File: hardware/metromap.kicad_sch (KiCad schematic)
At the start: 36 parts, among them J1 USB_C_Receptacle_USB2.0_16P, U1 AZ1117-3.3, U2 SN74LVC1G125DBV, U3 ESP32-C6-MINI-1-H4

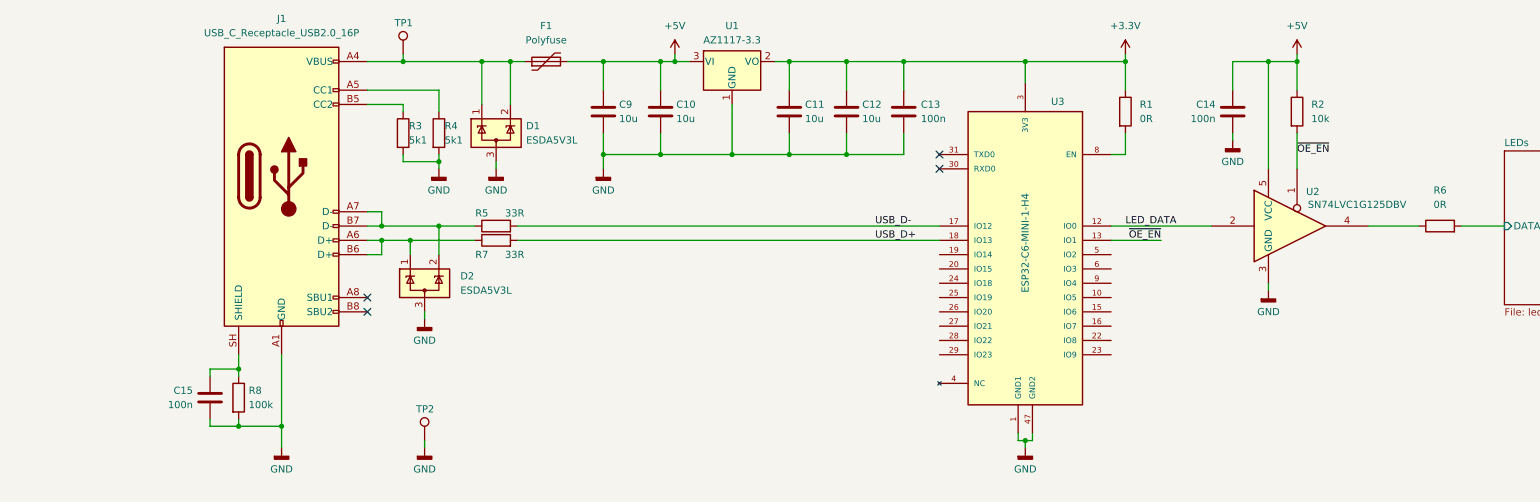
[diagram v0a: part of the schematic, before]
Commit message: Updated LED footprint
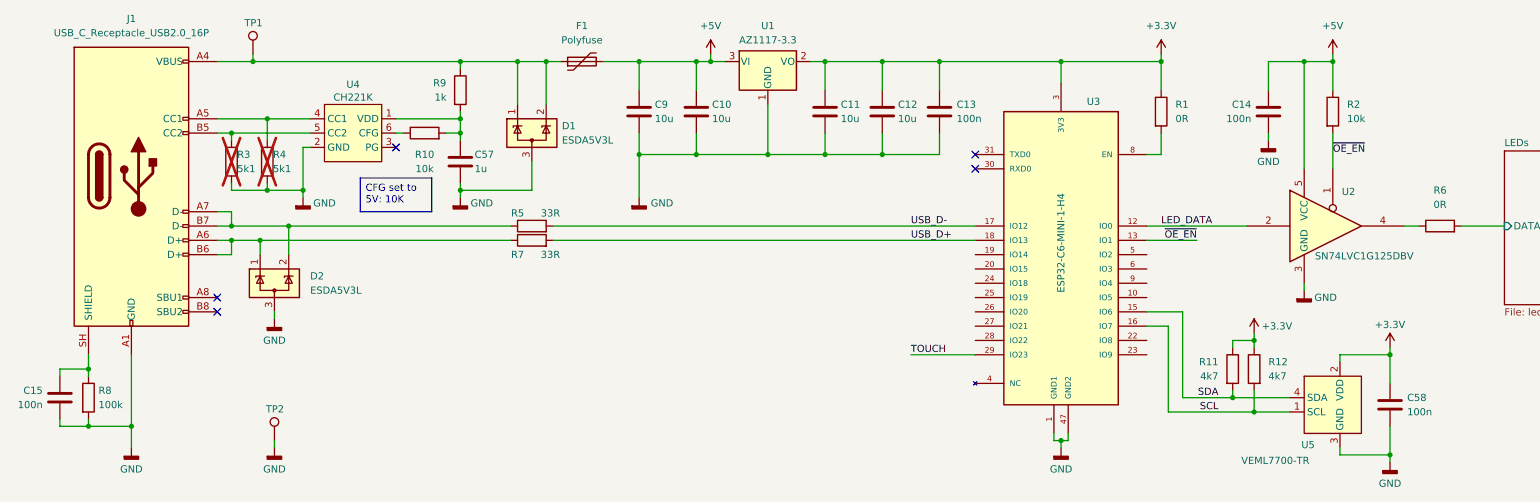
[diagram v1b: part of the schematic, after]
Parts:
- added C57: 1u, Capacitor_SMD:C_0603_1608Metric, symbol Device:C
- added C58: 100n, Capacitor_SMD:C_0402_1005Metric, symbol Device:C
- added R10: 10k, Resistor_SMD:R_0603_1608Metric, symbol Device:R
- added R11, R12: 4k7, Resistor_SMD:R_0603_1608Metric, symbol Device:R
- added R9: 1k, Resistor_SMD:R_0603_1608Metric, symbol Device:R
- added U4: CH221K, Package_TO_SOT_SMD:SOT-23-6, symbol metro-tracker:CH221K
- added U5: VEML7700-TR, metro-tracker:XDCR_VEML7700-TR, symbol metro-tracker:VEML7700-TR
- R3, R4: now not fitted
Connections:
- net +3.3V: now also C58.1, R11.1, R12.1, U5.2 (VDD)
- net GND: now also C57.2, C58.2, U4.2 (GND), U5.3 (GND)
- net at D1.1 (K), D1.2 (K), F1.1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: now also R9.1
- net at J1.A5 (CC1), R4.1: now also U4.4 (CC1)
- net at J1.B5 (CC2), R3.1: now also U4.5 (CC2)
- net SDA: now reaches U3.15 (IO6)
- net SDA: now also R11.2, U5.4 (SDA)
- net SCL: now reaches U3.16 (IO7)
- net SCL: now also R12.2, U5.1 (SCL)
- net TOUCH: now reaches U3.29 (IO23)
- new net: C57.1, R10.2, R9.2, U4.1 (VDD)
- new net: R10.1, U4.6 (CFG)
- no-connect marks 4 -> 5
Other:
- moved on the sheet: C10, C11, C12, C13, C14, C15, C9, D1, D2, F1, J1, R1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

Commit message: replaced buffer
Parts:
- removed U2: SN74LVC1G125DBV, Package_TO_SOT_SMD:SOT-23-5, symbol 74xGxx:SN74LVC1G125DBV
- added TP3, TP4: (no value), TestPoint:TestPoint_Pad_D2.0mm, symbol Connector:TestPoint
- added U2: SN74AHCT1G125DBVR, Package_TO_SOT_SMD:SOT-23-5, symbol metro-tracker:SN74AHCT1G125DBVR
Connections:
- net +5V: now also U2.5 (VCC)
- net GND: now also U2.3 (GND)
- net LED_DATA: now also U2.2
- net CON_USB_D+: now reaches J1.A6 (D+), J1.B6 (D+), R7.1
- net CON_USB_D+: now also D2.2 (K); no longer D2.1 (K)
- net CON_USB_D-: now reaches J1.A7 (D-), J1.B7 (D-), R5.1
- net CON_USB_D-: now also D2.1 (K); no longer D2.2 (K)
- net at R6.1: now also TP3.1, U2.4
- net ~{OE_EN} renamed ~{OE}
- net ~{OE}: now also TP4.1, U2.1

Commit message: Initial routing done
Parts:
- added C59: 47u, Capacitor_SMD:CP_Elec_6.3x7.7, symbol Device:C_Polarized
- C8: footprint Capacitor_SMD:CP_Elec_5x5.7 -> Capacitor_SMD:CP_Elec_6.3x7.7
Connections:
- net +5V: now also C59.1
- net GND: now also C59.2
- net VBUS: now reaches D1.1 (K), D1.2 (K), F1.1, J1.A4 (VBUS), J1.A9 (VBUS), J1.B4 (VBUS), J1.B9 (VBUS), R9.1, TP1.1
- net SH: now reaches C15.1, J1.SH (SHIELD), R8.1
- net TOUCH: no longer names the net of U3.29 (IO23)
- no-connect marks 5 -> 19
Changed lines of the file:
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@@
 	)
 	(no_connect
+		(at 186.69 109.22)
+	)
+	(no_connect
+		(at 186.69 101.6)
+	)
+	(no_connect
+		(at 186.69 93.98)
+	)
+	(no_connect
+		(at 217.17 96.52)
+	)
+	(no_connect
 		(at 186.69 76.2)
 	)
@@
 	)
 	(no_connect
+		(at 217.17 91.44)
+	)
+	(no_connect
+		(at 186.69 106.68)
+	)
+	(no_connect
+		(at 186.69 99.06)
+	)
+	(no_connect
+		(at 186.69 96.52)
+	)
+	(no_connect
 		(at 52.07 101.6)
 	)
 	(no_connect
+		(at 186.69 104.14)
+	)
+	(no_connect
+		(at 217.17 93.98)
+	)
+	(no_connect
+		(at 217.17 109.22)
+	)
+	(no_connect
 		(at 52.07 99.06)
 	)
 	(no_connect
+		(at 217.17 99.06)
+	)
+	(no_connect
+		(at 217.17 106.68)
+	)
+	(no_connect
+		(at 186.69 91.44)
+	)
+	(no_connect
 		(at 83.82 72.39)
 	)
@@
 	(wire
 		(pts
-			(xy 29.21 111.76) (xy 24.13 111.76)
+			(xy 389.89 68.58) (xy 389.89 69.85)
 		)
 		(stroke
@@
 	(wire
 		(pts
-			(xy 52.07 67.31) (xy 60.96 67.31)
+			(xy 29.21 111.76) (xy 24.13 111.76)
 		)
 		(stroke
@@
 	(wire
 		(pts
-			(xy 120.65 57.15) (xy 127 57.15)
+			(xy 52.07 67.31) (xy 60.96 67.31)
 		)
 		(stroke
@@
 	(wire
 		(pts
-			(xy 250.19 57.15) (xy 245.11 57.15)
+			(xy 120.65 57.15) (xy 127 57.15)
 		)
 		(stroke
@@
 	(wire
 		(pts
-			(xy 29.21 121.92) (xy 36.83 121.92)
+			(xy 250.19 57.15) (xy 245.11 57.15)
 		)
 		(stroke
@@
 	(wire
 		(pts
-			(xy 157.48 57.15) (xy 160.02 57.15)
+			(xy 29.21 121.92) (xy 36.83 121.92)
 		)
 		(stroke
@@
 	(wire
 		(pts
-			(xy 175.26 109.22) (xy 186.69 109.22)
+			(xy 157.48 57.15) (xy 160.02 57.15)
 		)
 		(stroke
@@
 	(wire
 		(pts
+			(xy 389.89 59.69) (xy 379.73 59.69)
+		)
+		(stroke
+			(width 0)
+			(type default)
+		)
+	)
+	(wire
+		(pts
 			(xy 52.07 86.36) (xy 54.61 86.36)
 		)
@@
 	(wire
 		(pts
+			(xy 389.89 69.85) (xy 379.73 69.85)
+		)
+		(stroke
+			(width 0)
+			(type default)
+		)
+	)
+	(wire
+		(pts
 			(xy 251.46 109.22) (xy 260.35 109.22)
 		)
@@
 		)
 	)
+	(wire
+		(pts
+			(xy 389.89 60.96) (xy 389.89 59.69)
+		)
+		(stroke
+			(width 0)
+			(type default)
+		)
+	)
 	(label "CON_USB_D-"
 		(at 69.85 86.36 0)
@@
 		)
 	)
-	(label "TOUCH"
-		(at 175.26 109.22 0)
-		(effects
-			(font
-				(size 1.27 1.27)
-			)
-			(justify left bottom)
-		)
-	)
 	(label "SDA"
 		(at 229.87 116.84 180)
@@
 		)
 	)
+	(label "SH"
+		(at 27.94 111.76 180)
+		(effects
+			(font
+				(size 1.27 1.27)
+			)
+			(justify right bottom)
+		)
+	)
+	(label "VBUS"
+		(at 63.5 57.15 0)
+		(effects
+			(font
+				(size 1.27 1.27)
+			)
+			(justify left bottom)
+		)
+	)
 	(label "~{OE}"
 		(at 250.19 74.93 0)
@@
 			)
 		)
-		(property "Footprint" "Capacitor_SMD:CP_Elec_5x5.7"
+		(property "Footprint" "Capacitor_SMD:CP_Elec_6.3x7.7"
 			(at 380.6952 68.58 0)
 			(hide yes)
@@
 					(unit 1)
 				)
+			)
+		)
+	)
+	(symbol
+		(lib_id "Device:C_Polarized")
+		(at 389.89 64.77 0)
+		(unit 1)
+		(body_style 1)
+		(exclude_from_sim no)
+		(in_bom yes)
+		(on_board yes)
+		(in_pos_files yes)
+		(dnp no)
+		(fields_autoplaced yes)
+		(property "Reference" "C59"
+			(at 393.7 62.6109 0)
+			(show_name no)
+			(do_not_autoplace no)
+			(effects
+				(font
+					(size 1.27 1.27)
+				)
+				(justify left)
+			)
+		)
+		(property "Value" "47u"
+			(at 393.7 65.1509 0)
+			(show_name no)
+			(do_not_autoplace no)
+			(effects
+				(font
+					(size 1.27 1.27)
+				)
+				(justify left)
+			)
+		)
+		(property "Footprint" "Capacitor_SMD:CP_Elec_6.3x7.7"
+			(at 390.8552 68.58 0)
+			(hide yes)
+			(show_name no)
+			(do_not_autoplace no)
+			(effects
+				(font
+					(size 1.27 1.27)
+				)
+			)
+		)
+		(property "Datasheet" ""
+			(at 389.89 64.77 0)
+			(hide yes)
+			(show_name no)
+			(do_not_autoplace no)
+			(effects
+				(font
+					(size 1.27 1.27)
+				)
+			)
+		)
+		(property "Description" "Polarized capacitor"
+			(at 389.89 64.77 0)
+			(hide yes)
+			(show_name no)
+			(do_not_autoplace no)
+			(effects
+				(font
+					(size 1.27 1.27)
+				)
+			)
+		)
+		(property "Digikey Part Number" "732-6390-1-ND"
+			(at 389.89 64.77 0)
+			(hide yes)
+			(show_name no)
+			(do_not_autoplace no)
+			(effects
+				(font
+					(size 1.27 1.27)
+				)
+			)
+		)
+		(property "JLCPCB Part Number" "C2161511"
+			(at 389.89 64.77 0)
+			(hide yes)
+			(show_name no)
+			(do_not_autoplace no)
+			(effects
+				(font
+					(size 1.27 1.27)
+				)
+			)
+		)
+		(property "Manufacturer Part Name JLCPCB" "16SVPG47M"
+			(at 389.89 64.77 0)
+			(hide yes)
+			(show_name no)
+			(do_not_autoplace no)
+			(effects
+				(font
+					(size 1.27 1.27)
+				)
+			)
+		)
+		(property "Manufacturer Part Number Digikey" "875105142001"
+			(at 389.89 64.77 0)
+			(hide yes)
+			(show_name no)
+			(do_not_autoplace no)
+			(effects
+				(font
+					(size 1.27 1.27)
+				)
+			)
+		)
+		(pin "1"
+		)
+		(pin "2"
+		)
+		(instances
+			(project "metromap"
+				(path "/933613dd-e874-4353-aa56-f5aedaa7dcf5"
+					(reference "C59")
+					(unit 1)
+				)

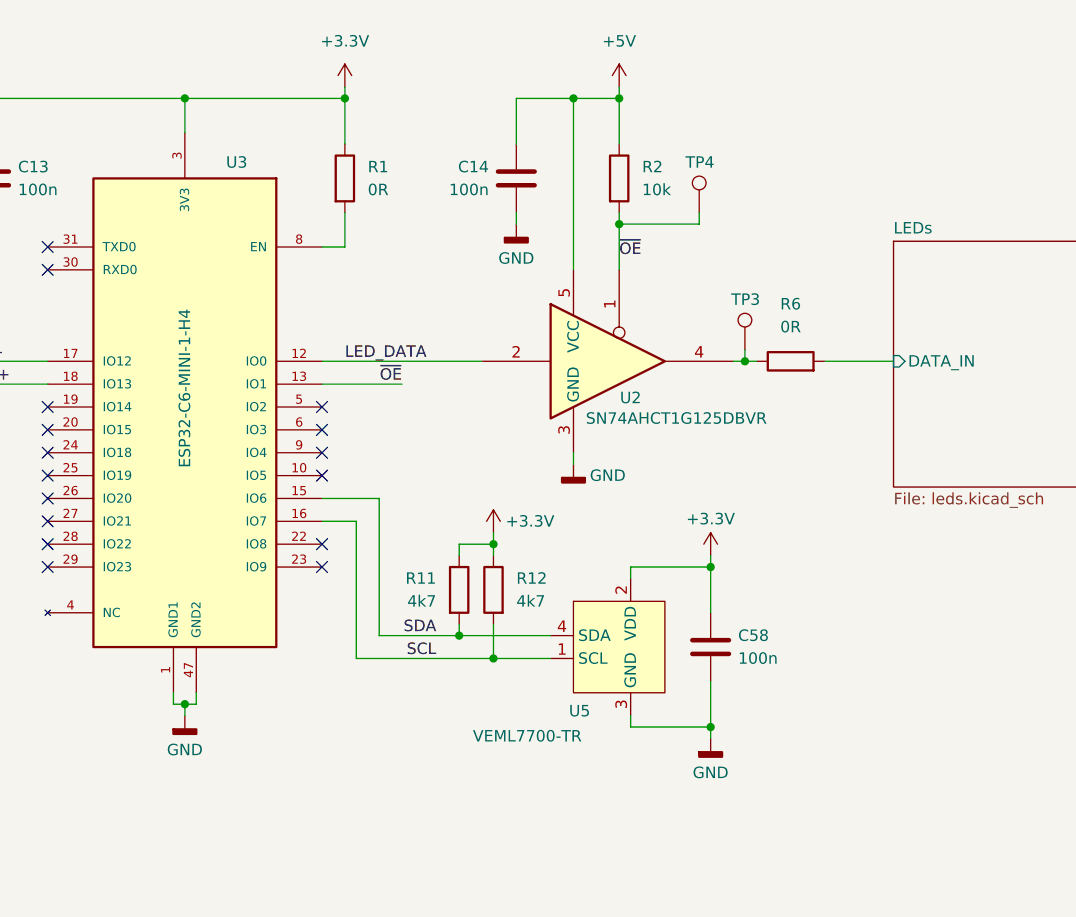
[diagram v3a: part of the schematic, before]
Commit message: added buttons
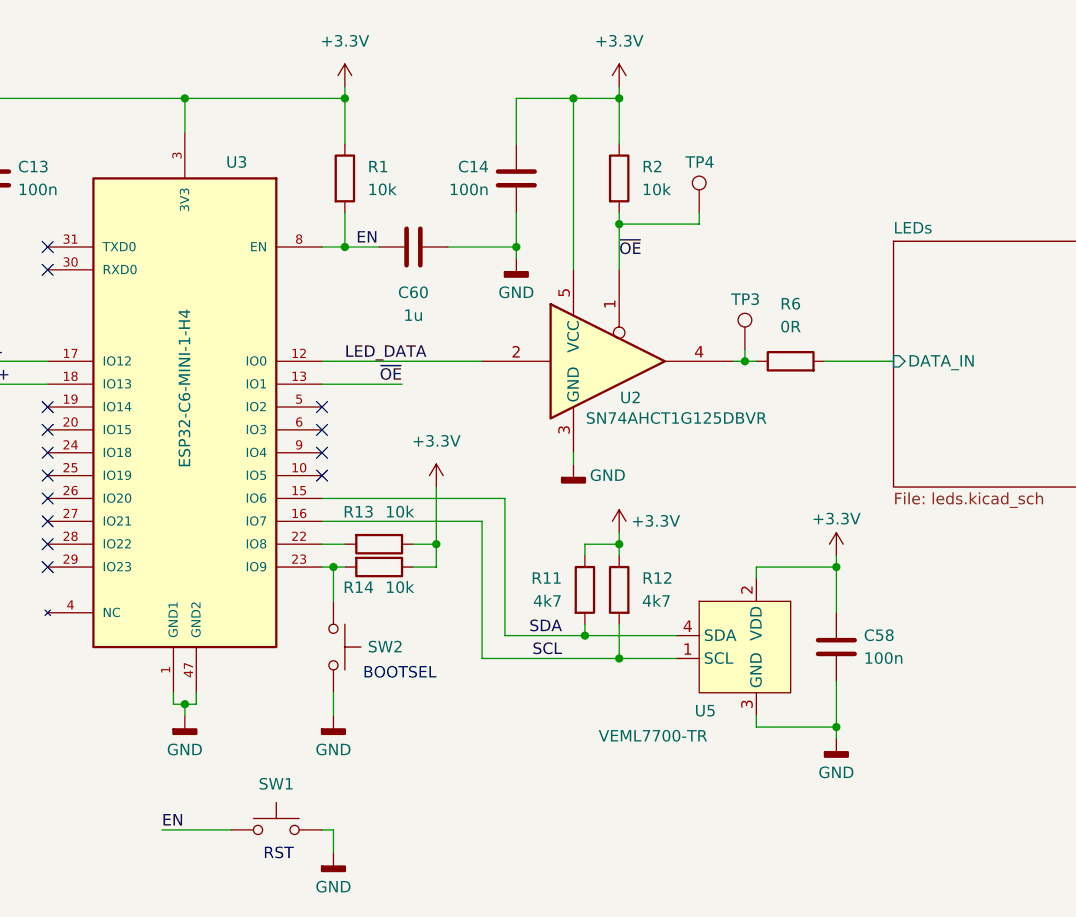
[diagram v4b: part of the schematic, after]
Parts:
- added C60: 1u, Capacitor_SMD:C_0603_1608Metric, symbol Device:C
- added R13, R14: 10k, Resistor_SMD:R_0603_1608Metric, symbol Device:R
- added SW1, SW2: XUNPU_TS-1088-AR02016, metro-tracker:TS-1088-AR02016, symbol metro-tracker:XUNPU_TS-1088-AR02016
- R1: value 0R -> 10k
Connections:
- net +3.3V: now also C14.1, R2.1, U2.5 (VCC), R13.1, R14.1
- net +5V: no longer C14.1, R2.1, U2.5 (VCC)
- net GND: now also C60.2, SW1.2, SW2.2
- net at U3.22 (IO8): now also R13.2
- net at U3.23 (IO9): now also R14.2, SW2.1
- net EN: now reaches R1.2, U3.8 (EN)
- net EN: now also C60.1, SW1.1
- no-connect marks 19 -> 17
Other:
- note added: "BOOTSEL"
- note added: "RST"
- moved on the sheet: C58, R11, R12, U5

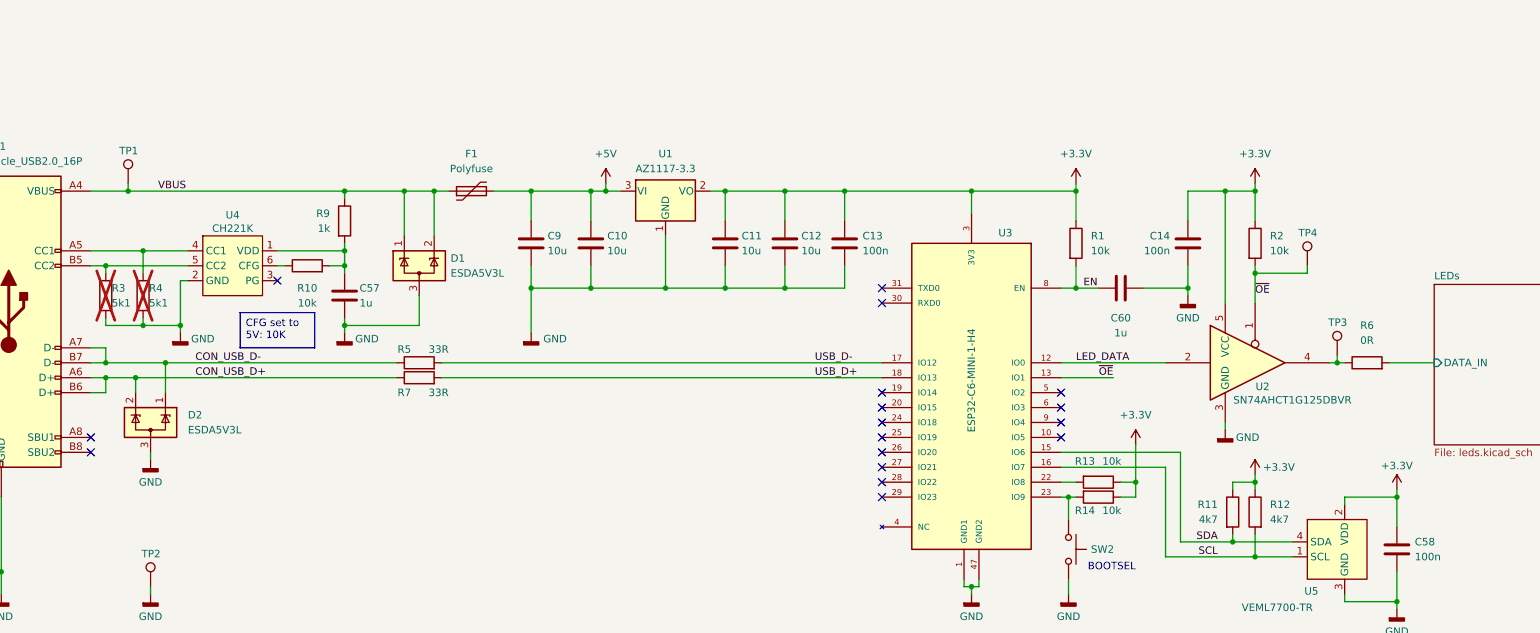
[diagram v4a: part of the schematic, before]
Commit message: Added backup LDO and fixed OE ref
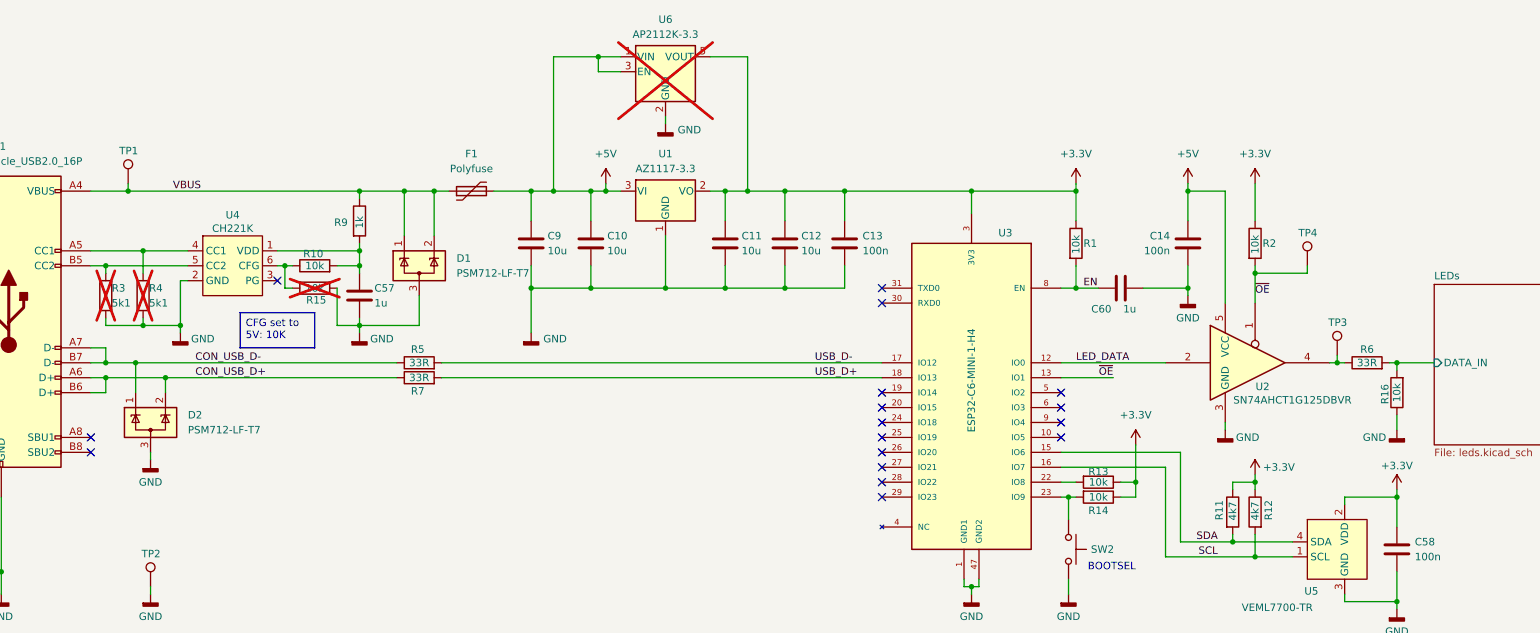
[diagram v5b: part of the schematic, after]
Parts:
- removed D1, D2: ESDA5V3L, Package_TO_SOT_SMD:SOT-23-3, symbol Power_Protection:ESDA5V3L
- added D1, D2: PSM712-LF-T7, Package_TO_SOT_SMD:SOT-23-3, symbol metro-tracker:PSM712-LF-T7
- added R15, R16: 10k, Resistor_SMD:R_0603_1608Metric, symbol Device:R
- added U6: AP2112K-3.3, Package_TO_SOT_SMD:SOT-23-5, symbol Regulator_Linear:AP2112K-3.3
- F1: footprint Fuse:Fuse_1812_4532Metric -> metro-tracker:Fuse_1812_4532Metric
- R6: value 0R -> 33R
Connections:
- net +3.3V: now also U6.5 (VOUT); no longer C14.1, U2.5 (VCC)
- net +5V: now also C14.1, U2.5 (VCC), U6.1 (VIN), U6.3 (EN)
- net CON_USB_D+: now also D2.2 (K)
- net CON_USB_D-: now also D2.1 (K)
- net GND: now also D1.3 (A), D2.3 (A), R15.1, R16.1, U6.2 (GND)
- net LEDs/DATA_IN: now also R16.2
- net VBUS: now also D1.1 (K), D1.2 (K)
- net at R10.1, U4.6 (CFG): now also R15.2
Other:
- moved on the sheet: C57, R10, R9

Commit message: fix tvs diodes
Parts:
- removed D1, D2: PSM712-LF-T7, Package_TO_SOT_SMD:SOT-23-3, symbol metro-tracker:PSM712-LF-T7
- added D1: P6SMB6.8CA/TR13, Diode_SMD:D_SMB, symbol Diode:SM6T6V8A
- added U7: SRV05-4, Package_TO_SOT_SMD:SOT-23-6, symbol Power_Protection:SRV05-4
- C59, C8: JLCPCB Part Number C2161511 -> C3339; Manufacturer Part Name JLCPCB 16SVPG47M -> RVT1V101M0607
- SW1, SW2: JLCPCB Part Number (none) -> C720477; Manufacturer Part Name JLCPCB (none) -> TS-1088-AR02016
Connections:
- net +5V: now also D1.1 (A1)
- net CON_USB_D+: now also U7.1 (IO1), U7.6 (IO4)
- net CON_USB_D-: now also U7.3 (IO2), U7.4 (IO3)
- net GND: now also D1.2 (A2), U7.2 (VN)
- net VBUS: now also U7.5 (VP)
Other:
- moved on the sheet: F1
